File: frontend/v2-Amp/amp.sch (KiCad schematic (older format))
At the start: 69 parts, among them K1 HK4100, P1 Antenna, P2 CONN_02X06, P4 TX-IN, P5 RX IN, P6 12-13.8v, Q1 PZT2222A, Q2 RD16HHF1, T1 OUT_TRANSF, T2 BN-43-2402, U1 LP2951-50D

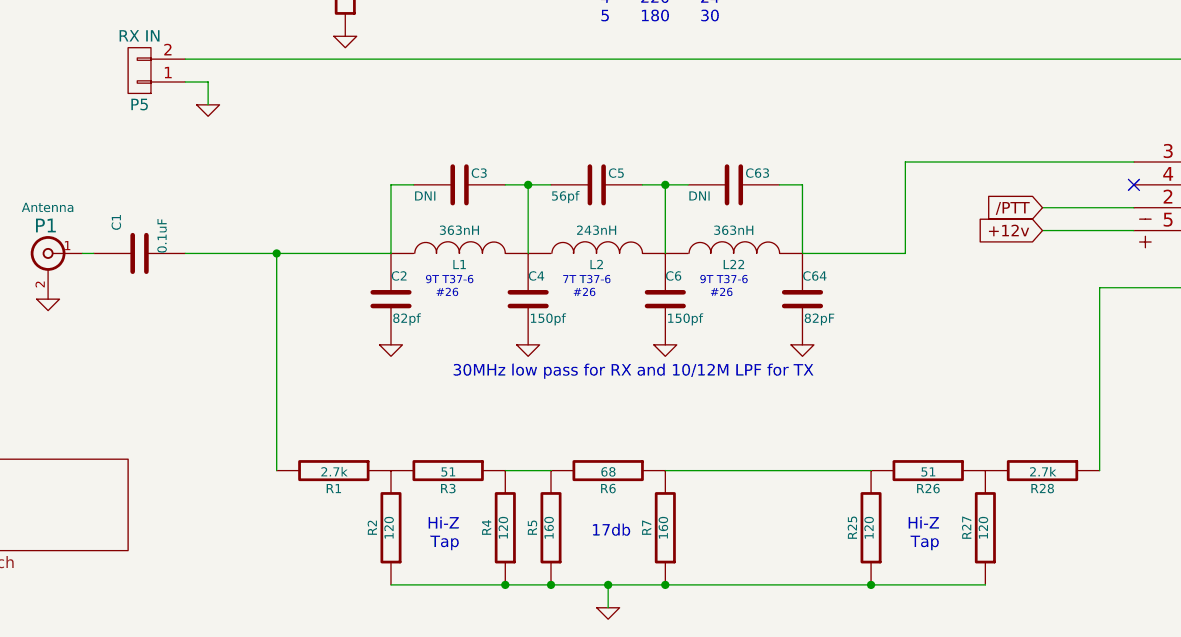
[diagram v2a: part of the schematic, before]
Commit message: Updates to pure signal tap
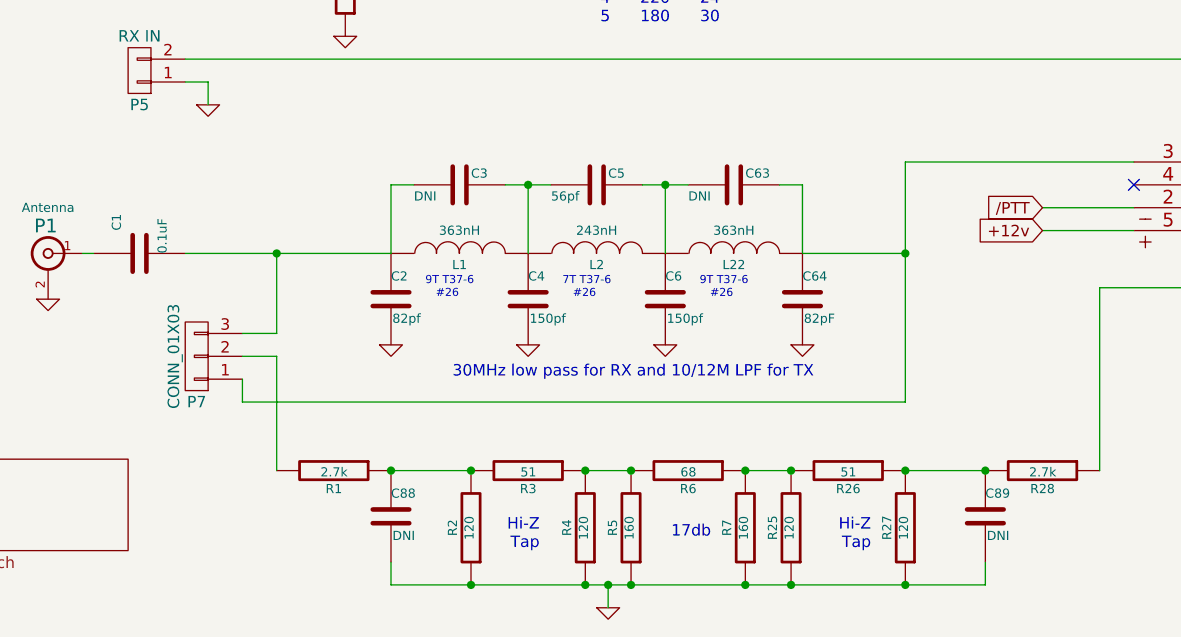
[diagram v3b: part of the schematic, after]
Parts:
- added C88, C89: DNI, HERMESLITE:C_0805, symbol C
- added P7: CONN_01X03, Pin_Headers:Pin_Header_Straight_1x03, symbol CONN_01X03
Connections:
- net GND: now also C88.2, C89.2
- net at C1.2, C2.1, C3.2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: now also P7.3 (P3); no longer R1.2
- net at C63.1, C64.1, K1.3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: now also P7.1 (P1)
- net at R1.1, R2.2, R3.2: now also C88.1
- net at R26.1, R27.2, R28.2: now also C89.1
- new net: P7.2 (P2), R1.2
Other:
- moved on the sheet: R2, R25, R26, R27, R3, R4, R5, R6, R7
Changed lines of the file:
@@
 L R R2
 U 1 1 55CFBB62
-P 2750 7450
-F 0 "R2" V 2830 7450 40  0000 C CNN
-F 1 "120" V 2757 7451 40  0000 C CNN
-F 2 "Resistors_SMD:R_0805_HandSoldering" V 2680 7450 30  0001 C CNN
-F 3 "" H 2750 7450 30  0000 C CNN
-	1    2750 7450
+P 3100 7450
+F 0 "R2" V 3180 7450 40  0000 C CNN
+F 1 "120" V 3107 7451 40  0000 C CNN
+F 2 "Resistors_SMD:R_0805_HandSoldering" V 3030 7450 30  0001 C CNN
+F 3 "" H 3100 7450 30  0000 C CNN
+	1    3100 7450
 	-1   0    0    1
 $EndComp
@@
 L R R3
 U 1 1 55CFBC8C
-P 3000 7200
-F 0 "R3" V 3080 7200 40  0000 C CNN
-F 1 "51" V 3007 7201 40  0000 C CNN
-F 2 "Resistors_SMD:R_0805_HandSoldering" V 2930 7200 30  0001 C CNN
-F 3 "" H 3000 7200 30  0000 C CNN
-	1    3000 7200
+P 3350 7200
+F 0 "R3" V 3430 7200 40  0000 C CNN
+F 1 "51" V 3357 7201 40  0000 C CNN
+F 2 "Resistors_SMD:R_0805_HandSoldering" V 3280 7200 30  0001 C CNN
+F 3 "" H 3350 7200 30  0000 C CNN
+	1    3350 7200
 	0    1    1    0
 $EndComp
@@
 L R R4
 U 1 1 55CFBCEB
-P 3250 7450
-F 0 "R4" V 3330 7450 40  0000 C CNN
-F 1 "120" V 3257 7451 40  0000 C CNN
-F 2 "Resistors_SMD:R_0805_HandSoldering" V 3180 7450 30  0001 C CNN
-F 3 "" H 3250 7450 30  0000 C CNN
-	1    3250 7450
+P 3600 7450
+F 0 "R4" V 3680 7450 40  0000 C CNN
+F 1 "120" V 3607 7451 40  0000 C CNN
+F 2 "Resistors_SMD:R_0805_HandSoldering" V 3530 7450 30  0001 C CNN
+F 3 "" H 3600 7450 30  0000 C CNN
+	1    3600 7450
 	-1   0    0    1
 $EndComp
@@
 L R R6
 U 1 1 55CFBDB2
-P 3700 7200
-F 0 "R6" V 3780 7200 40  0000 C CNN
-F 1 "68" V 3707 7201 40  0000 C CNN
-F 2 "Resistors_SMD:R_0805_HandSoldering" V 3630 7200 30  0001 C CNN
-F 3 "" H 3700 7200 30  0000 C CNN
-	1    3700 7200
+P 4050 7200
+F 0 "R6" V 4130 7200 40  0000 C CNN
+F 1 "68" V 4057 7201 40  0000 C CNN
+F 2 "Resistors_SMD:R_0805_HandSoldering" V 3980 7200 30  0001 C CNN
+F 3 "" H 4050 7200 30  0000 C CNN
+	1    4050 7200
 	0    1    1    0
 $EndComp
@@
 L R R5
 U 1 1 55CFBE60
-P 3450 7450
-F 0 "R5" V 3530 7450 40  0000 C CNN
-F 1 "160" V 3457 7451 40  0000 C CNN
-F 2 "Resistors_SMD:R_0805_HandSoldering" V 3380 7450 30  0001 C CNN
-F 3 "" H 3450 7450 30  0000 C CNN
-	1    3450 7450
-	-1   0    0    1
-$EndComp
-Wire Wire Line
-	3250 7200 3450 7200
+P 3800 7450
+F 0 "R5" V 3880 7450 40  0000 C CNN
+F 1 "160" V 3807 7451 40  0000 C CNN
+F 2 "Resistors_SMD:R_0805_HandSoldering" V 3730 7450 30  0001 C CNN
+F 3 "" H 3800 7450 30  0000 C CNN
+	1    3800 7450
+	-1   0    0    1
+$EndComp
+Wire Wire Line
+	3600 7200 3800 7200
 $Comp
 L R R7
 U 1 1 55CFBF51
-P 3950 7450
-F 0 "R7" V 4030 7450 40  0000 C CNN
-F 1 "160" V 3957 7451 40  0000 C CNN
-F 2 "Resistors_SMD:R_0805_HandSoldering" V 3880 7450 30  0001 C CNN
-F 3 "" H 3950 7450 30  0000 C CNN
-	1    3950 7450
-	-1   0    0    1
-$EndComp
-Text Notes 3800 7500 2    50   ~ 0
+P 4300 7450
+F 0 "R7" V 4380 7450 40  0000 C CNN
+F 1 "160" V 4307 7451 40  0000 C CNN
+F 2 "Resistors_SMD:R_0805_HandSoldering" V 4230 7450 30  0001 C CNN
+F 3 "" H 4300 7450 30  0000 C CNN
+	1    4300 7450
+	-1   0    0    1
+$EndComp
+Text Notes 4150 7500 2    50   ~ 0
 17db
-Wire Wire Line
-	3950 7200 4850 7200
-Wire Wire Line
-	2750 7700 5350 7700
-Connection ~ 3950 7700
-Connection ~ 3450 7700
-Connection ~ 3250 7700
+Connection ~ 4500 7200
+Connection ~ 3600 7700
+Connection ~ 3100 7700
 Wire Wire Line
 	3700 7700 3700 7800
@@
 	6000 5850 5000 5850
 Wire Wire Line
-	5000 5850 5000 6250
-Wire Wire Line
-	2250 6250 2250 7200
+	5000 5850 5000 6900
 Connection ~ 2250 6250
 $Comp
@@
 Text Notes 1700 1700 0    50   ~ 0
 Common
-Text Notes 3050 7550 2    50   ~ 0
+Text Notes 3400 7550 2    50   ~ 0
 Hi-Z\nTap
 Connection ~ 5700 2600
@@
 L R R25
 U 1 1 55E06206
-P 4850 7450
-F 0 "R25" V 4930 7450 40  0000 C CNN
-F 1 "120" V 4857 7451 40  0000 C CNN
-F 2 "Resistors_SMD:R_0805_HandSoldering" V 4780 7450 30  0001 C CNN
-F 3 "" H 4850 7450 30  0000 C CNN
-	1    4850 7450
+P 4500 7450
+F 0 "R25" V 4580 7450 40  0000 C CNN
+F 1 "120" V 4507 7451 40  0000 C CNN
+F 2 "Resistors_SMD:R_0805_HandSoldering" V 4430 7450 30  0001 C CNN
+F 3 "" H 4500 7450 30  0000 C CNN
+	1    4500 7450
 	-1   0    0    1
 $EndComp
@@
 L R R26
 U 1 1 55E063F6
-P 5100 7200
-F 0 "R26" V 5180 7200 40  0000 C CNN
-F 1 "51" V 5107 7201 40  0000 C CNN
-F 2 "Resistors_SMD:R_0805_HandSoldering" V 5030 7200 30  0001 C CNN
-F 3 "" H 5100 7200 30  0000 C CNN
-	1    5100 7200
+P 4750 7200
+F 0 "R26" V 4830 7200 40  0000 C CNN
+F 1 "51" V 4757 7201 40  0000 C CNN
+F 2 "Resistors_SMD:R_0805_HandSoldering" V 4680 7200 30  0001 C CNN
+F 3 "" H 4750 7200 30  0000 C CNN
+	1    4750 7200
 	0    1    1    0
 $EndComp
@@
 L R R27
 U 1 1 55E06491
-P 5350 7450
-F 0 "R27" V 5430 7450 40  0000 C CNN
-F 1 "120" V 5357 7451 40  0000 C CNN
-F 2 "Resistors_SMD:R_0805_HandSoldering" V 5280 7450 30  0001 C CNN
-F 3 "" H 5350 7450 30  0000 C CNN
-	1    5350 7450
+P 5000 7450
+F 0 "R27" V 5080 7450 40  0000 C CNN
+F 1 "120" V 5007 7451 40  0000 C CNN
+F 2 "Resistors_SMD:R_0805_HandSoldering" V 4930 7450 30  0001 C CNN
+F 3 "" H 5000 7450 30  0000 C CNN
+	1    5000 7450
 	-1   0    0    1
 $EndComp
@@
 	0    1    1    0
 $EndComp
-Connection ~ 4850 7700
-Text Notes 5150 7550 2    50   ~ 0
+Connection ~ 5000 7700
+Text Notes 4850 7550 2    50   ~ 0
 Hi-Z\nTap
 Wire Wire Line
@@
 Wire Wire Line
 	1450 4550 1750 4550
+$Comp
+L CONN_01X03 P7
+U 1 1 55EC9B26
+P 1900 6700
+F 0 "P7" H 1900 6900 50  0000 C CNN
+F 1 "CONN_01X03" V 2000 6700 50  0000 C CNN
+F 2 "Pin_Headers:Pin_Header_Straight_1x03" H 1900 6700 60  0001 C CNN
+F 3 "" H 1900 6700 60  0000 C CNN
+	1    1900 6700
+	-1   0    0    1
+$EndComp
+Wire Wire Line
+	2100 6700 2250 6700
+Wire Wire Line
+	2250 6700 2250 7200
+Wire Wire Line
+	2100 6600 2250 6600
+Wire Wire Line
+	2250 6600 2250 6250
+Wire Wire Line
+	2100 6800 2100 6900
+Wire Wire Line
+	2100 6900 5000 6900
+Connection ~ 5000 6250
+$Comp
+L C C88
+U 1 1 55ECA6D8
+P 2750 7400
+F 0 "C88" H 2750 7500 40  0000 L CNN
+F 1 "DNI" H 2756 7315 40  0000 L CNN
+F 2 "HERMESLITE:C_0805" H 2788 7250 30  0001 C CNN
+F 3 "" H 2750 7400 60  0000 C CNN
+	1    2750 7400
+	1    0    0    -1
+$EndComp
+$Comp
+L C C89
+U 1 1 55ECAAB4
+P 5350 7400
+F 0 "C89" H 5350 7500 40  0000 L CNN
+F 1 "DNI" H 5356 7315 40  0000 L CNN
+F 2 "HERMESLITE:C_0805" H 5388 7250 30  0001 C CNN
+F 3 "" H 5350 7400 60  0000 C CNN
+	1    5350 7400
+	1    0    0    -1
+$EndComp
+Wire Wire Line
+	5350 7700 5350 7600
+Wire Wire Line
+	5000 7200 5350 7200
+Connection ~ 3800 7700
+Wire Wire Line
+	4300 7200 4500 7200
+Wire Wire Line
+	3100 7200 2750 7200
+Wire Wire Line
+	2750 7600 2750 7700
+Connection ~ 4500 7700
+Connection ~ 4300 7700
+Connection ~ 4300 7200
+Connection ~ 5000 7200
+Connection ~ 5350 7200
+Connection ~ 3800 7200
+Connection ~ 3600 7200
+Connection ~ 3100 7200
+Connection ~ 2750 7200
+Wire Wire Line
+	2750 7700 5350 7700
 $EndSCHEMATC

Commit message: 1.0 fab version
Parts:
- removed R25, R4: 120, Resistors_SMD:R_0805_HandSoldering, symbol R
- added P3: Tap Enable, Pin_Headers:Pin_Header_Straight_1x02, symbol CONN_01X02
- P7: value CONN_01X03 -> Tap Source
- R5, R7: value 160 -> 68
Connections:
- net at K1.1, P5.2 (P2): now also P3.1 (P1); no longer R28.1
- new net: P3.2 (P2), R28.1
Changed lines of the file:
@@
-$EndComp
-$Comp
-L R R4
-U 1 1 55CFBCEB
-P 3600 7450
-F 0 "R4" V 3680 7450 40  0000 C CNN
-F 1 "120" V 3607 7451 40  0000 C CNN
-F 2 "Resistors_SMD:R_0805_HandSoldering" V 3530 7450 30  0001 C CNN
-F 3 "" H 3600 7450 30  0000 C CNN
-	1    3600 7450
-	-1   0    0    1
 $EndComp
 $Comp
@@
 P 3800 7450
 F 0 "R5" V 3880 7450 40  0000 C CNN
-F 1 "160" V 3807 7451 40  0000 C CNN
+F 1 "68" V 3807 7451 40  0000 C CNN
 F 2 "Resistors_SMD:R_0805_HandSoldering" V 3730 7450 30  0001 C CNN
 F 3 "" H 3800 7450 30  0000 C CNN
@@
 P 4300 7450
 F 0 "R7" V 4380 7450 40  0000 C CNN
-F 1 "160" V 4307 7451 40  0000 C CNN
+F 1 "68" V 4307 7451 40  0000 C CNN
 F 2 "Resistors_SMD:R_0805_HandSoldering" V 4230 7450 30  0001 C CNN
 F 3 "" H 4300 7450 30  0000 C CNN
@@
 Text Notes 4150 7500 2    50   ~ 0
 17db
-Connection ~ 4500 7200
-Connection ~ 3600 7700
 Connection ~ 3100 7700
 Wire Wire Line
@@
 $EndComp
 $Comp
-L R R25
-U 1 1 55E06206
-P 4500 7450
-F 0 "R25" V 4580 7450 40  0000 C CNN
-F 1 "120" V 4507 7451 40  0000 C CNN
-F 2 "Resistors_SMD:R_0805_HandSoldering" V 4430 7450 30  0001 C CNN
-F 3 "" H 4500 7450 30  0000 C CNN
-	1    4500 7450
-	-1   0    0    1
-$EndComp
-$Comp
 L R R26
 U 1 1 55E063F6
@@
 Hi-Z\nTap
 Wire Wire Line
-	5850 7200 5850 6400
-Wire Wire Line
-	5850 6400 7100 6400
+	7100 6400 5850 6400
 $Comp
 L R R14
@@
 P 1900 6700
 F 0 "P7" H 1900 6900 50  0000 C CNN
-F 1 "CONN_01X03" V 2000 6700 50  0000 C CNN
+F 1 "Tap Source" V 2000 6700 50  0000 C CNN
 F 2 "Pin_Headers:Pin_Header_Straight_1x03" H 1900 6700 60  0001 C CNN
 F 3 "" H 1900 6700 60  0000 C CNN
@@
 Wire Wire Line
 	2750 7600 2750 7700
-Connection ~ 4500 7700
 Connection ~ 4300 7700
 Connection ~ 4300 7200
@@
 Connection ~ 5350 7200
 Connection ~ 3800 7200
-Connection ~ 3600 7200
 Connection ~ 3100 7200
 Connection ~ 2750 7200
 Wire Wire Line
 	2750 7700 5350 7700
+$Comp
+L CONN_01X02 P3
+U 1 1 55ECC21D
+P 6050 6650
+F 0 "P3" H 6050 6800 50  0000 C CNN
+F 1 "Tap Enable" V 6150 6650 50  0000 C CNN
+F 2 "Pin_Headers:Pin_Header_Straight_1x02" H 6050 6650 60  0001 C CNN
+F 3 "" H 6050 6650 60  0000 C CNN
+	1    6050 6650
+	1    0    0    -1
+$EndComp
+Wire Wire Line
+	5850 7200 5850 6700
+Wire Wire Line
+	5850 6400 5850 6600
 $EndSCHEMATC

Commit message: Starting V1.1 updates
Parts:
- removed C2: 82pf, HERMESLITE:C_0805, symbol C
- removed C3, C63: DNI, HERMESLITE:C_0805, symbol C
- removed C4, C6: 150pf, HERMESLITE:C_0805, symbol C
- removed C5: 56pf, HERMESLITE:C_0805, symbol C
- removed C64: 82pF, HERMESLITE:C_0805, symbol C
- removed L1, L22: 363nH, HERMESLITE:Choke_Toroid, symbol INDUCTOR
- removed L2: 243nH, HERMESLITE:Choke_Toroid, symbol INDUCTOR
- removed P7: Tap Source, Pin_Headers:Pin_Header_Straight_1x03, symbol CONN_01X03
- P3: value Tap Enable -> TX Power Tap
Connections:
- net GND: now also P3.1 (P1)
- net at C1.2: now also K1.3, R1.2
- net at K1.1, P5.2 (P2): no longer P3.1 (P1)
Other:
- note removed: "30MHz low pass for RX and 10/12M LPF for TX"
- note removed: "7T T37-6\n #26"
- note removed: "9T T37-6\n #26"
- moved on the sheet: P3

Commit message: Filter updates
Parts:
- added C2: 82pf, HERMESLITE:C_0805, symbol C
- added C3, C63: DNI, HERMESLITE:C_0805, symbol C
- added C4, C6: 150pf, HERMESLITE:C_0805, symbol C
- added C5: 56pf, HERMESLITE:C_0805, symbol C
- added C64: 82pF, HERMESLITE:C_0805, symbol C
- added L1, L22: 363nH, HERMESLITE:Choke_Toroid, symbol INDUCTOR
- added L2: 243nH, HERMESLITE:Choke_Toroid, symbol INDUCTOR
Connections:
- net GND: now also C2.2, C4.2, C6.2, C64.2
- net at C1.2, R1.2: now also C2.1, C3.2, L1.1; no longer K1.3
- new net: C63.1, C64.1, K1.3, L22.2
- new net: C3.1, C4.1, C5.2, L1.2, L2.1
- new net: C5.1, C6.1, C63.2, L2.2, L22.1
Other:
- note added: "30MHz low pass for RX and 10/12M LPF for TX"
- note added: "8T T37-6\n6in #26"
- note added: "9T T37-6\n7in #26"
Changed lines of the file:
@@
 $EndComp
 Wire Wire Line
-	1850 6250 5000 6250
-Wire Wire Line
-	5000 6250 5000 5850
+	5000 5850 5000 6250
 Wire Wire Line
 	7100 5750 7100 5400
@@
 	5850 7700 5850 7450
 Connection ~ 5350 7700
+Text Notes 2850 6800 0    50   ~ 0
+30MHz low pass for RX and 10/12M LPF for TX
+$Comp
+L INDUCTOR L1
+U 1 1 560EC0EC
+P 3150 6250
+F 0 "L1" V 3100 6250 40  0000 C CNN
+F 1 "363nH" V 3250 6250 40  0000 C CNN
+F 2 "HERMESLITE:Choke_Toroid" H 3150 6250 60  0001 C CNN
+F 3 "" H 3150 6250 60  0000 C CNN
+	1    3150 6250
+	0    -1   -1   0
+$EndComp
+$Comp
+L INDUCTOR L2
+U 1 1 560EC0F3
+P 3750 6250
+F 0 "L2" V 3700 6250 40  0000 C CNN
+F 1 "243nH" V 3850 6250 40  0000 C CNN
+F 2 "HERMESLITE:Choke_Toroid" H 3750 6250 60  0001 C CNN
+F 3 "" H 3750 6250 60  0000 C CNN
+	1    3750 6250
+	0    -1   -1   0
+$EndComp
+$Comp
+L C C2
+U 1 1 560EC0FA
+P 2850 6450
+F 0 "C2" H 2850 6550 40  0000 L CNN
+F 1 "82pf" H 2856 6365 40  0000 L CNN
+F 2 "HERMESLITE:C_0805" H 2888 6300 30  0001 C CNN
+F 3 "" H 2850 6450 60  0000 C CNN
+	1    2850 6450
+	1    0    0    -1
+$EndComp
+$Comp
+L C C4
+U 1 1 560EC101
+P 3450 6450
+F 0 "C4" H 3450 6550 40  0000 L CNN
+F 1 "150pf" H 3456 6365 40  0000 L CNN
+F 2 "HERMESLITE:C_0805" H 3488 6300 30  0001 C CNN
+F 3 "" H 3450 6450 60  0000 C CNN
+	1    3450 6450
+	1    0    0    -1
+$EndComp
+$Comp
+L C C6
+U 1 1 560EC108
+P 4050 6450
+F 0 "C6" H 4050 6550 40  0000 L CNN
+F 1 "150pf" H 4056 6365 40  0000 L CNN
+F 2 "HERMESLITE:C_0805" H 4088 6300 30  0001 C CNN
+F 3 "" H 4050 6450 60  0000 C CNN
+	1    4050 6450
+	1    0    0    -1
+$EndComp
+$Comp
+L GND #PWR028
+U 1 1 560EC10F
+P 2850 6650
+F 0 "#PWR028" H 2850 6650 30  0001 C CNN
+F 1 "GND" H 2850 6580 30  0001 C CNN
+F 2 "" H 2850 6650 60  0000 C CNN
+F 3 "" H 2850 6650 60  0000 C CNN
+	1    2850 6650
+	1    0    0    -1
+$EndComp
+$Comp
+L GND #PWR029
+U 1 1 560EC115
+P 3450 6650
+F 0 "#PWR029" H 3450 6650 30  0001 C CNN
+F 1 "GND" H 3450 6580 30  0001 C CNN
+F 2 "" H 3450 6650 60  0000 C CNN
+F 3 "" H 3450 6650 60  0000 C CNN
+	1    3450 6650
+	1    0    0    -1
+$EndComp
+$Comp
+L GND #PWR030
+U 1 1 560EC11B
+P 4050 6650
+F 0 "#PWR030" H 4050 6650 30  0001 C CNN
+F 1 "GND" H 4050 6580 30  0001 C CNN
+F 2 "" H 4050 6650 60  0000 C CNN
+F 3 "" H 4050 6650 60  0000 C CNN
+	1    4050 6650
+	1    0    0    -1
+$EndComp
+$Comp
+L C C3
+U 1 1 560EC121
+P 3150 5950
+F 0 "C3" V 3100 6000 40  0000 L CNN
+F 1 "DNI" V 3200 5750 40  0000 L CNN
+F 2 "HERMESLITE:C_0805" H 3188 5800 30  0001 C CNN
+F 3 "" H 3150 5950 60  0000 C CNN
+	1    3150 5950
+	0    1    1    0
+$EndComp
+$Comp
+L C C5
+U 1 1 560EC128
+P 3750 5950
+F 0 "C5" V 3700 6000 40  0000 L CNN
+F 1 "56pf" V 3800 5750 40  0000 L CNN
+F 2 "HERMESLITE:C_0805" H 3788 5800 30  0001 C CNN
+F 3 "" H 3750 5950 60  0000 C CNN
+	1    3750 5950
+	0    1    1    0
+$EndComp
+Wire Wire Line
+	2850 6250 2850 5950
+Wire Wire Line
+	2850 5950 2950 5950
+Wire Wire Line
+	3950 5950 4150 5950
+Wire Wire Line
+	4050 5950 4050 6250
+Wire Wire Line
+	3450 5950 3450 6250
+Connection ~ 3450 5950
+Text Notes 3600 6450 0    35   ~ 0
+9T T37-6\n7in #26
+Text Notes 3000 6450 0    35   ~ 0
+8T T37-6\n6in #26
+$Comp
+L INDUCTOR L22
+U 1 1 560EC137
+P 4350 6250
+F 0 "L22" V 4300 6250 40  0000 C CNN
+F 1 "363nH" V 4450 6250 40  0000 C CNN
+F 2 "HERMESLITE:Choke_Toroid" H 4350 6250 60  0001 C CNN
+F 3 "" H 4350 6250 60  0000 C CNN
+	1    4350 6250
+	0    -1   -1   0
+$EndComp
+$Comp
+L C C64
+U 1 1 560EC13E
+P 4650 6450
+F 0 "C64" H 4650 6550 40  0000 L CNN
+F 1 "82pF" H 4656 6365 40  0000 L CNN
+F 2 "HERMESLITE:C_0805" H 4688 6300 30  0001 C CNN
+F 3 "" H 4650 6450 60  0000 C CNN
+	1    4650 6450
+	1    0    0    -1
+$EndComp
+$Comp
+L C C63
+U 1 1 560EC145
+P 4350 5950
+F 0 "C63" V 4300 6000 40  0000 L CNN
+F 1 "DNI" V 4400 5750 40  0000 L CNN
+F 2 "HERMESLITE:C_0805" H 4388 5800 30  0001 C CNN
+F 3 "" H 4350 5950 60  0000 C CNN
+	1    4350 5950
+	0    1    1    0
+$EndComp
+Wire Wire Line
+	3350 5950 3550 5950
+Connection ~ 4050 5950
+Wire Wire Line
+	4550 5950 4650 5950
+Wire Wire Line
+	4650 5950 4650 6250
+$Comp
+L GND #PWR031
+U 1 1 560EC150
+P 4650 6650
+F 0 "#PWR031" H 4650 6650 30  0001 C CNN
+F 1 "GND" H 4650 6580 30  0001 C CNN
+F 2 "" H 4650 6650 60  0000 C CNN
+F 3 "" H 4650 6650 60  0000 C CNN
+	1    4650 6650
+	1    0    0    -1
+$EndComp
+Text Notes 4200 6450 0    35   ~ 0
+8T T37-6\n6in #26
+Wire Wire Line
+	1850 6250 2850 6250
+Wire Wire Line
+	4650 6250 5000 6250
 $EndSCHEMATC
